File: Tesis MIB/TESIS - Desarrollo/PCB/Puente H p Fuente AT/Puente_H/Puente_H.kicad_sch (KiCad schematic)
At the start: 86 parts, among them J1 Vfb+, J10 PIN_+12V, J11 PIN_GND, J12 PIN_+5V, J13 Screw_Terminal_01x04, J14 Screw_Terminal_01x03, J2 Vfb-, J3 Screw_Terminal_01x02, J4 Screw_Terminal_01x02, J5 Vfb, J6 PB_ICout, J7 PA_ICout, J8 PB_BDin, J9 PA_BDin, Q1 BC547, Q2 BC547, Q3 BC337, Q4 IRF3205, Q5 IRF3205, Q6 IRF3205, Q7 IRF3205, Q8 BC547, Q9 BC547, T1 Transformer_1P_1S, U1 NA555P, U2 4N27, U3 4N27, U4 SG3525, U5 LM7805_TO220, U6 4N27, U7 4N27

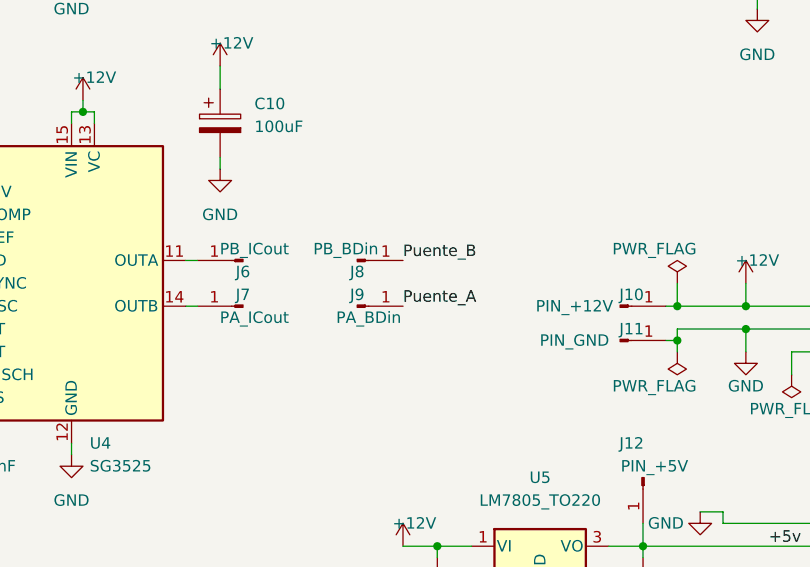
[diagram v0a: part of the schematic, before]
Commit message: Acualización del CAP2
Finalización de la 1ra parte del CAP2, redacción de titulos y subtitulos para esquematizar los CAP3 y CAP4, actualización de los indices de Contenidos, Tablas y Figuras y Referencias insertadas (hasta la 48).
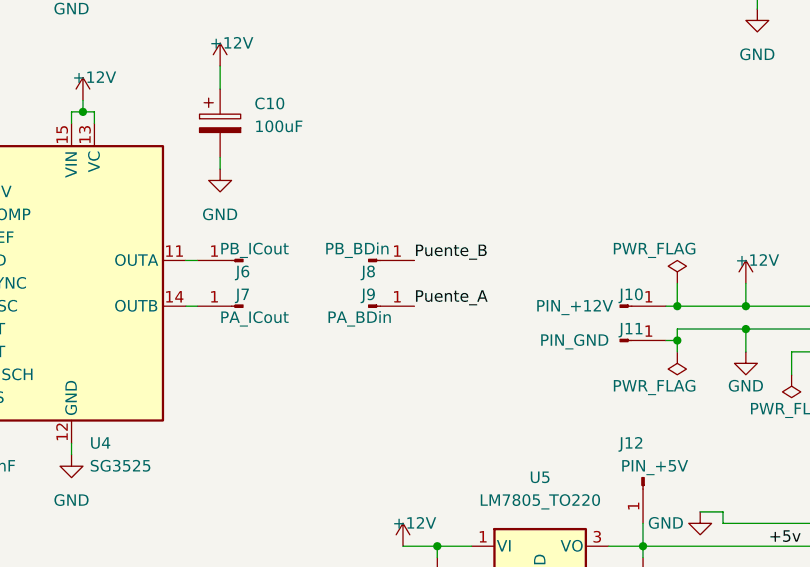
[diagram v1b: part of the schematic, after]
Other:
- moved on the sheet: J8, J9

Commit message: Actualiza CAP 2 parcial 2
Actualiza el documento de tesis con el CAP 2 casi finalizado, solo resto agregar "Simulaciones" y cierre final.
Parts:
- removed R17: 5k1, Resistor_THT:R_Axial_DIN0207_L6.3mm_D2.5mm_P7.62mm_Horizontal, symbol Device:R
- added RV2: 10k, Potentiometer_THT:Potentiometer_Bourns_3296W_Vertical, symbol Device:R_Potentiometer
- RV1: value R_Potentiometer -> 1k
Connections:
- net GND: now also RV2.2
- net at R21.1, U4.2 (NI): now also RV2.3
- net +300v renamed +Vat
- net -300v renamed -Vat
- no-connect marks 7 -> 8
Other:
- moved on the sheet: C10, C7, C8, C9, J3, J4, J5, J6, J7, J8, J9, R18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

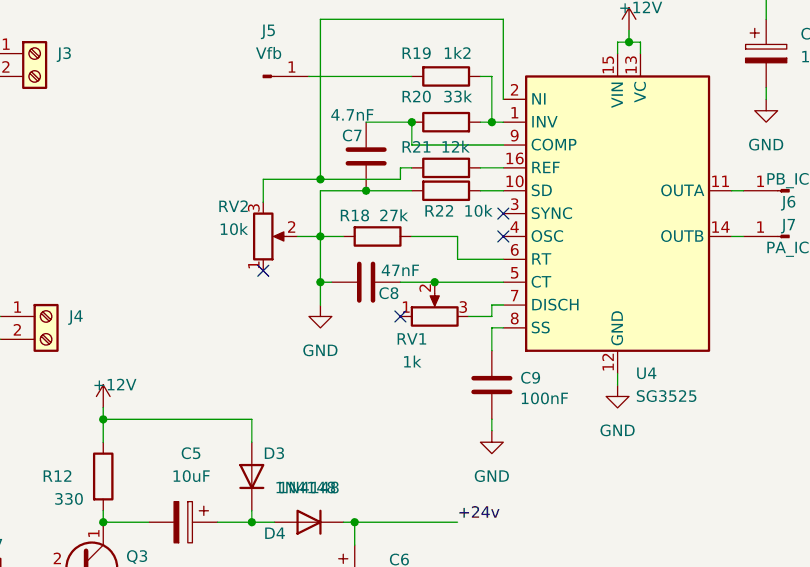
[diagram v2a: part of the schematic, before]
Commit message: Actualiza Pruebas
Agrega planilla, gráficos y capturas del osciloscopio para el CAP3
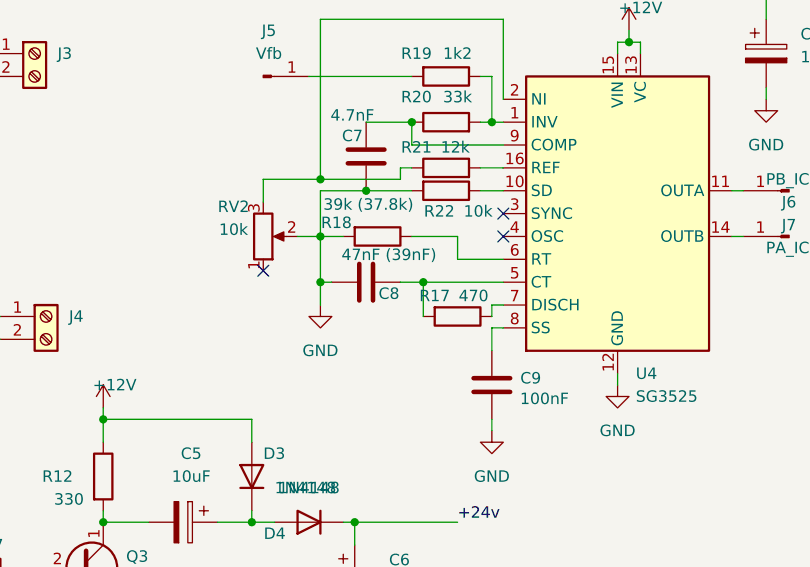
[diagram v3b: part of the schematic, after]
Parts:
- removed RV1: 1k, Potentiometer_THT:Potentiometer_Bourns_3296W_Vertical, symbol Device:R_Potentiometer
- added R17: 470, Resistor_THT:R_Axial_DIN0207_L6.3mm_D2.5mm_P7.62mm_Horizontal, symbol Device:R
- C8: value 47nF -> 47nF (39nF)
- R18: value 27k -> 39k (37.8k)
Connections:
- net at C8.2, U4.5 (CT): now also R17.2
- net at U4.7 (DISCH): now also R17.1
- no-connect marks 8 -> 7
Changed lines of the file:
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@@
 	)
 	(junction
+		(at 121.92 129.54)
+		(diameter 0)
+		(color 0 0 0 0)
+	)
+	(junction
 		(at 129.54 111.76)
 		(diameter 0)
@@
 	)
 	(junction
-		(at 123.19 129.54)
-		(diameter 0)
-		(color 0 0 0 0)
-	)
-	(junction
 		(at 115.57 119.38)
 		(diameter 0)
@@
 	)
 	(no_connect
-		(at 119.38 133.35)
-	)
-	(no_connect
 		(at 130.81 124.46)
 	)
@@
 	(wire
 		(pts
+			(xy 121.92 129.54) (xy 121.92 133.35)
+		)
+		(stroke
+			(width 0)
+			(type default)
+		)
+	)
+	(wire
+		(pts
 			(xy 219.71 140.97) (xy 231.14 140.97)
 		)
@@
 	(wire
 		(pts
-			(xy 127 133.35) (xy 129.54 133.35)
-		)
-		(stroke
-			(width 0)
-			(type default)
-		)
-	)
-	(wire
-		(pts
 			(xy 115.57 111.76) (xy 120.65 111.76)
 		)
@@
 	(wire
 		(pts
-			(xy 119.38 129.54) (xy 123.19 129.54)
-		)
-		(stroke
-			(width 0)
-			(type default)
-		)
-	)
-	(wire
-		(pts
 			(xy 45.72 139.7) (xy 57.15 139.7)
 		)
@@
 	(wire
 		(pts
-			(xy 123.19 129.54) (xy 130.81 129.54)
+			(xy 119.38 129.54) (xy 121.92 129.54)
 		)
 		(stroke
@@
 	(wire
 		(pts
+			(xy 121.92 129.54) (xy 130.81 129.54)
+		)
+		(stroke
+			(width 0)
+			(type default)
+		)
+	)
+	(wire
+		(pts
 			(xy 30.48 107.95) (xy 35.56 107.95)
 		)
@@
 	)
 	(symbol
+		(lib_id "Device:R")
+		(at 125.73 133.35 270)
+		(unit 1)
+		(exclude_from_sim no)
+		(in_bom yes)
+		(on_board yes)
+		(dnp no)
+		(property "Reference" "R17"
+			(at 123.19 131.064 90)
+			(effects
+				(font
+					(size 1.27 1.27)
+				)
+			)
+		)
+		(property "Value" "470"
+			(at 127.508 131.064 90)
+			(effects
+				(font
+					(size 1.27 1.27)
+				)
+			)
+		)
+		(property "Footprint" "Resistor_THT:R_Axial_DIN0207_L6.3mm_D2.5mm_P7.62mm_Horizontal"
+			(at 125.73 131.572 90)
+			(effects
+				(font
+					(size 1.27 1.27)
+				)
+				(hide yes)
+			)
+		)
+		(property "Datasheet" "~"
+			(at 125.73 133.35 0)
+			(effects
+				(font
+					(size 1.27 1.27)
+				)
+				(hide yes)
+			)
+		)
+		(property "Description" ""
+			(at 125.73 133.35 0)
+			(effects
+				(font
+					(size 1.27 1.27)
+				)
+				(hide yes)
+			)
+		)
+		(pin "1"
+		)
+		(pin "2"
+		)
+		(instances
+			(project "Puente_H"
+				(path "/557348b5-6217-4385-bfe3-5dcdd45f2644"
+					(reference "R17")
+					(unit 1)
+				)
+			)
+		)
+	)
+	(symbol
 		(lib_id "power:+5V")
 		(at 215.9 34.29 0)
@@
 	)
 	(symbol
-		(lib_id "Device:R_Potentiometer")
-		(at 123.19 133.35 90)
-		(unit 1)
-		(exclude_from_sim no)
-		(in_bom yes)
-		(on_board yes)
-		(dnp no)
-		(property "Reference" "RV1"
-			(at 120.65 135.89 90)
-			(effects
-				(font
-					(size 1.27 1.27)
-				)
-			)
-		)
-		(property "Value" "1k"
-			(at 120.65 138.43 90)
-			(effects
-				(font
-					(size 1.27 1.27)
-				)
-			)
-		)
-		(property "Footprint" "Potentiometer_THT:Potentiometer_Bourns_3296W_Vertical"
-			(at 123.19 133.35 0)
-			(effects
-				(font
-					(size 1.27 1.27)
-				)
-				(hide yes)
-			)
-		)
-		(property "Datasheet" "~"
-			(at 123.19 133.35 0)
-			(effects
-				(font
-					(size 1.27 1.27)
-				)
-				(hide yes)
-			)
-		)
-		(property "Description" ""
-			(at 123.19 133.35 0)
-			(effects
-				(font
-					(size 1.27 1.27)
-				)
-				(hide yes)
-			)
-		)
-		(pin "1"
-		)
-		(pin "2"
-		)
-		(pin "3"
-		)
-		(instances
-			(project "Puente_H"
-				(path "/557348b5-6217-4385-bfe3-5dcdd45f2644"
-					(reference "RV1")
-					(unit 1)
-				)
-			)
-		)
-	)
-	(symbol
 		(lib_id "Device:R")
 		(at 57.15 153.67 270)
@@
 			)
 		)
-		(property "Value" "47nF"
-			(at 119.38 128.27 90)
+		(property "Value" "47nF (39nF)"
+			(at 118.11 126.492 90)
 			(effects
 				(font
@@
 		(dnp no)
 		(property "Reference" "R18"
-			(at 114.3 122.174 90)
+			(at 112.268 122.936 90)
 			(effects
 				(font
@@
 			)
 		)
-		(property "Value" "27k"
-			(at 118.618 122.174 90)
+		(property "Value" "39k (37.8k)"
+			(at 115.824 120.904 90)
 			(effects
 				(font

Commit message: CAP 3 finalizado e inicio del 4to
Redactado la discución de resultados
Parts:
- R13, R14, R25, R26: value 4k7 -> 1k
- R15, R16, R23, R24: value 10k -> 2k2
- R17: value 470 -> 3k
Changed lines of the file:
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@@
 			)
 		)
-		(property "Value" "10k"
+		(property "Value" "2k2"
 			(at 111.76 80.01 90)
 			(effects
@@
 			)
 		)
-		(property "Value" "10k"
+		(property "Value" "2k2"
 			(at 113.03 54.61 90)
 			(effects
@@
 		(on_board yes)
 		(dnp no)
-		(fields_autoplaced yes)
 		(property "Reference" "#PWR011"
 			(at 110.49 138.43 0)
@@
 		)
 		(property "Value" "GND"
-			(at 110.49 137.16 0)
+			(at 108.458 135.89 0)
 			(effects
 				(font
@@
 		(dnp no)
 		(property "Reference" "R17"
-			(at 123.19 131.064 90)
+			(at 126.238 135.89 90)
 			(effects
 				(font
@@
 			)
 		)
-		(property "Value" "470"
-			(at 127.508 131.064 90)
+		(property "Value" "3k"
+			(at 126.238 138.176 90)
 			(effects
 				(font
@@
 		(dnp no)
 		(property "Reference" "R13"
-			(at 102.87 62.23 90)
+			(at 104.14 60.706 0)
 			(effects
 				(font
@@
 			)
 		)
-		(property "Value" "4k7"
-			(at 102.87 66.04 90)
+		(property "Value" "1k"
+			(at 103.378 62.992 0)
 			(effects
 				(font
@@
 			)
 		)
-		(property "Value" "10k"
+		(property "Value" "2k2"
 			(at 186.69 80.01 90)
 			(effects
@@
 			)
 		)
-		(property "Value" "4k7"
+		(property "Value" "1k"
 			(at 105.156 34.798 0)
 			(effects
@@
 			)
 		)
-		(property "Value" "10k"
+		(property "Value" "2k2"
 			(at 186.69 54.61 90)
 			(effects
@@
 		(dnp no)
 		(property "Reference" "C8"
-			(at 118.11 130.81 90)
+			(at 113.538 133.096 90)
 			(effects
 				(font
@@
 		)
 		(property "Value" "47nF (39nF)"
-			(at 118.11 126.492 90)
+			(at 118.11 135.636 90)
 			(effects
 				(font
@@
 			)
 		)
-		(property "Value" "4k7"
+		(property "Value" "1k"
 			(at 199.39 31.75 90)
 			(effects
@@
 		(dnp no)
 		(property "Reference" "R18"
-			(at 112.268 122.936 90)
+			(at 116.332 122.428 90)
 			(effects
 				(font
@@
 		)
 		(property "Value" "39k (37.8k)"
-			(at 115.824 120.904 90)
+			(at 118.618 126.746 90)
 			(effects
 				(font
@@
 			)
 		)
-		(property "Value" "4k7"
+		(property "Value" "1k"
 			(at 199.39 58.42 90)
 			(effects
